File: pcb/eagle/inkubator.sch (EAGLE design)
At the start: 34 parts, among them Q1 BT138-600, Q2 BT138-600, U1 L78L33ABUTR, U2 MOC3063, U3 MOC3063

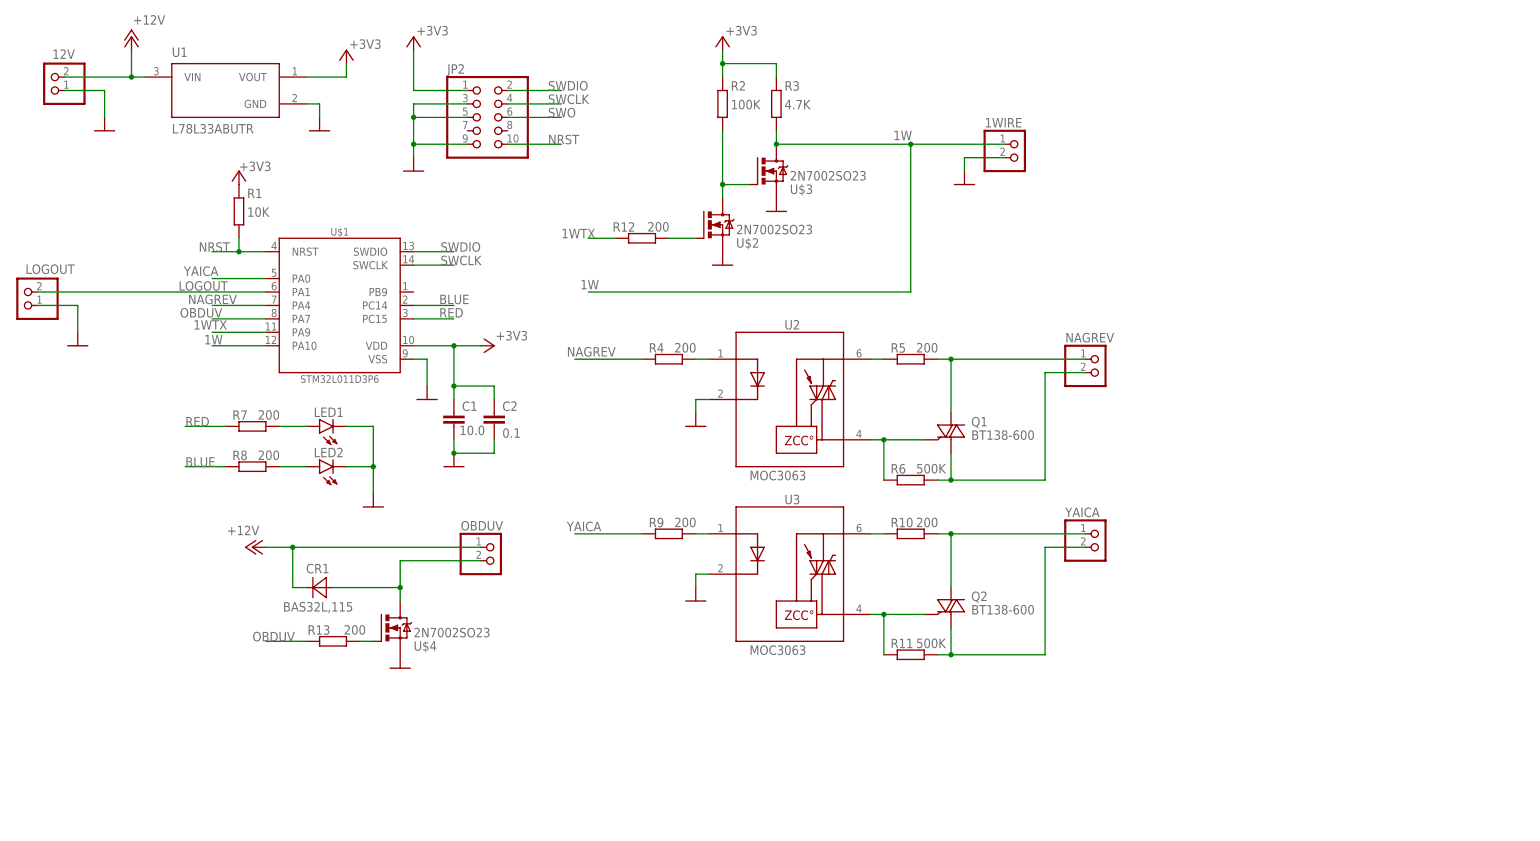
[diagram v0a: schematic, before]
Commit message: Рефакторинг принципиальной схемы и печатной платы
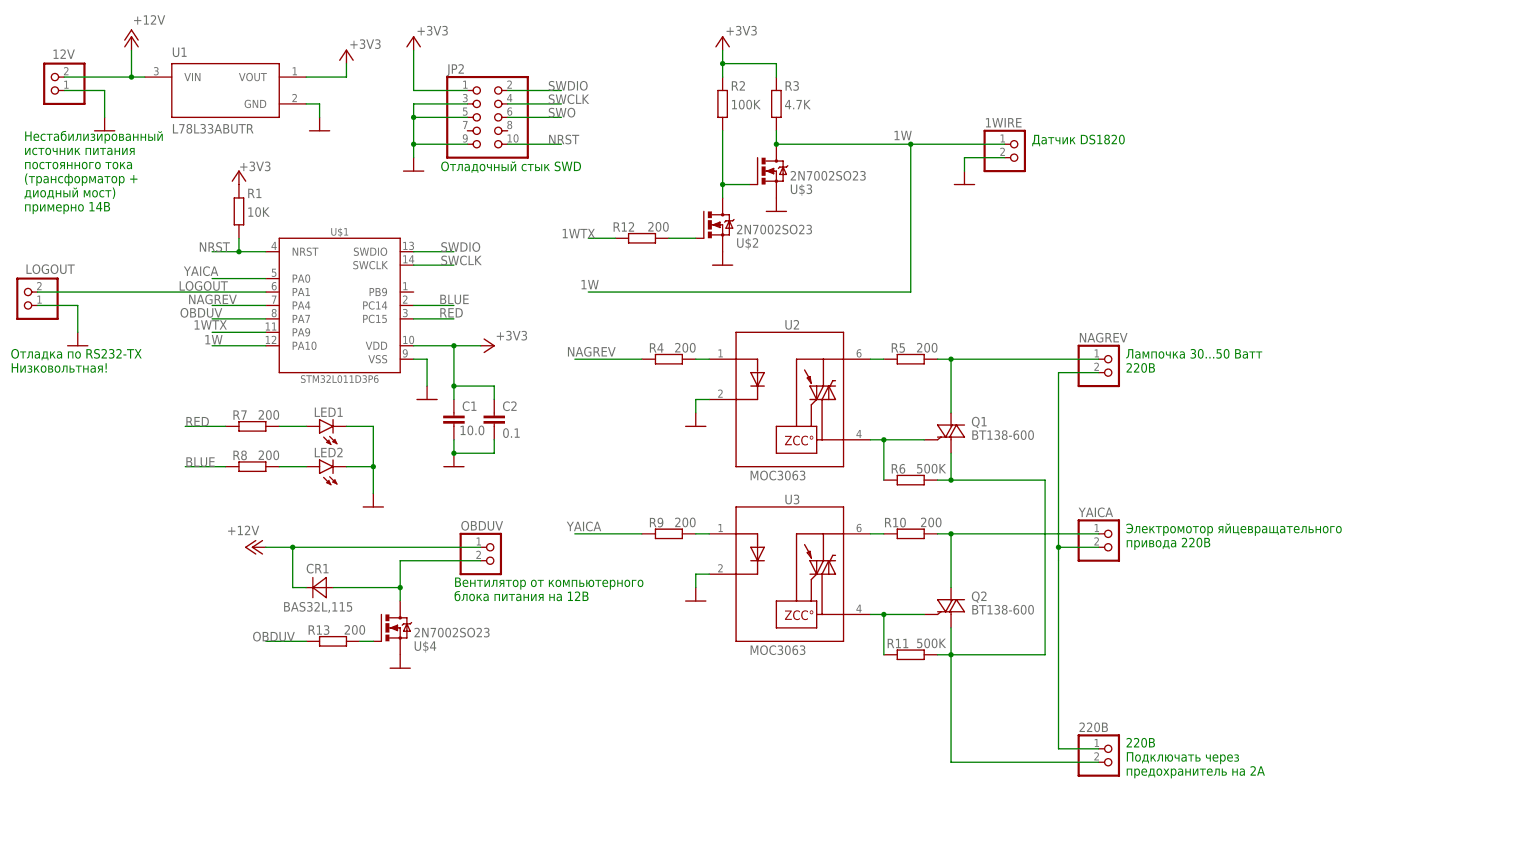
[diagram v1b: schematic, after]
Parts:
- added 220В: (no value), pinhead:PINHD-1X2
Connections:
- net N$13: now also 220В.2, Q1.A1, R6.1; no longer YAICA.2
- net N$6: now also 220В.1, YAICA.2; no longer Q1.A1, R6.1
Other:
- note added: "220В Подключать через предохранитель на 2А"
- note added: "Вентилятор от компьютерного блока питания на 12В"
- note added: "Датчик DS1820"
- note added: "Лампочка 30...50 Ватт 220В"
- note added: "Нестабилизированный источник питания постоянного тока (трансформатор + диодный мост) примерно 14В"
- note added: "Отладка по RS232-TX Низковольтная!"
- note added: "Отладочный стык SWD"
- note added: "Электромотор яйцевращательного привода 220В"
- moved on the sheet: NAGREV, YAICA
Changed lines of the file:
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@@
 <part name="LOGOUT" library="pinhead" library_urn="urn:adsk.eagle:library:325" deviceset="PINHD-1X2" device="" package3d_urn="urn:adsk.eagle:package:22435/2"/>
 <part name="GND13" library="supply1" library_urn="urn:adsk.eagle:library:371" deviceset="GND" device=""/>
+<part name="220В" library="pinhead" library_urn="urn:adsk.eagle:library:325" deviceset="PINHD-1X2" device="" package3d_urn="urn:adsk.eagle:package:22435/2"/>
 </parts>
 <sheets>
 <sheet>
 <plain>
+<text x="193.04" y="55.88" size="1.778" layer="91">Лампочка 30...50 Ватт
+220В</text>
+<text x="193.04" y="22.86" size="1.778" layer="91">Электромотор яйцевращательного
+привода 220В</text>
+<text x="175.26" y="99.06" size="1.778" layer="91">Датчик DS1820</text>
+<text x="66.04" y="12.7" size="1.778" layer="91">Вентилятор от компьютерного
+блока питания на 12В</text>
+<text x="-17.78" y="55.88" size="1.778" layer="91">Отладка по RS232-TX
+Низковольтная!</text>
+<text x="-15.24" y="86.36" size="1.778" layer="91">Нестабилизированный
+источник питания
+постоянного тока
+(трансформатор +
+диодный мост)
+примерно 14В</text>
+<text x="63.5" y="93.98" size="1.778" layer="91">Отладочный стык SWD</text>
+<text x="193.04" y="-20.32" size="1.778" layer="91">220В
+Подключать через
+предохранитель на 2А</text>
 </plain>
 <instances>
@@
 </instance>
 <instance part="GND8" gate="1" x="162.56" y="91.44" smashed="yes"/>
-<instance part="NAGREV" gate="G$1" x="187.96" y="55.88" smashed="yes">
-<attribute name="NAME" x="181.61" y="61.595" size="1.778" layer="95"/>
-<attribute name="VALUE" x="181.61" y="50.8" size="1.778" layer="96"/>
+<instance part="NAGREV" gate="G$1" x="190.5" y="55.88" smashed="yes">
+<attribute name="NAME" x="184.15" y="61.595" size="1.778" layer="95"/>
+<attribute name="VALUE" x="184.15" y="50.8" size="1.778" layer="96"/>
 </instance>
 <instance part="U3" gate="G$1" x="129.54" y="17.78" smashed="yes">
@@
 </instance>
 <instance part="R10" gate="G$1" x="152.4" y="25.4" smashed="yes" rot="R180">
-<attribute name="NAME" x="148.59" y="26.6446" size="1.778" layer="95"/>
-<attribute name="VALUE" x="153.416" y="26.67" size="1.778" layer="96"/>
+<attribute name="NAME" x="147.32" y="26.6446" size="1.778" layer="95"/>
+<attribute name="VALUE" x="154.178" y="26.67" size="1.778" layer="96"/>
 </instance>
 <instance part="R11" gate="G$1" x="152.4" y="2.54" smashed="yes" rot="R180">
-<attribute name="NAME" x="148.59" y="3.7846" size="1.778" layer="95"/>
+<attribute name="NAME" x="147.828" y="3.7846" size="1.778" layer="95"/>
 <attribute name="VALUE" x="153.416" y="3.81" size="1.778" layer="96"/>
 </instance>
-<instance part="YAICA" gate="G$1" x="187.96" y="22.86" smashed="yes">
-<attribute name="NAME" x="181.61" y="28.575" size="1.778" layer="95"/>
-<attribute name="VALUE" x="181.61" y="17.78" size="1.778" layer="96"/>
+<instance part="YAICA" gate="G$1" x="190.5" y="22.86" smashed="yes">
+<attribute name="NAME" x="184.15" y="28.575" size="1.778" layer="95"/>
+<attribute name="VALUE" x="184.15" y="17.78" size="1.778" layer="96"/>
 </instance>
 <instance part="U$4" gate="G$1" x="53.34" y="7.62" smashed="yes" rot="MR180">
@@
 </instance>
 <instance part="GND13" gate="1" x="-5.08" y="60.96" smashed="yes"/>
+<instance part="220В" gate="G$1" x="190.5" y="-17.78" smashed="yes">
+<attribute name="NAME" x="184.15" y="-12.065" size="1.778" layer="95"/>
+<attribute name="VALUE" x="184.15" y="-22.86" size="1.778" layer="96"/>
+</instance>
 </instances>
 <busses>
@@
 <pinref part="Q1" gate="G$1" pin="A2"/>
 <wire x1="160.02" y1="58.42" x2="160.02" y2="48.26" width="0.1524" layer="91"/>
-<wire x1="160.02" y1="58.42" x2="185.42" y2="58.42" width="0.1524" layer="91"/>
+<wire x1="160.02" y1="58.42" x2="187.96" y2="58.42" width="0.1524" layer="91"/>
 <junction x="160.02" y="58.42"/>
 <pinref part="NAGREV" gate="G$1" pin="1"/>
-</segment>
-</net>
-<net name="N$6" class="0">
-<segment>
-<pinref part="R6" gate="G$1" pin="1"/>
-<wire x1="157.48" y1="35.56" x2="160.02" y2="35.56" width="0.1524" layer="91"/>
-<pinref part="Q1" gate="G$1" pin="A1"/>
-<wire x1="160.02" y1="35.56" x2="160.02" y2="40.64" width="0.1524" layer="91"/>
-<wire x1="160.02" y1="35.56" x2="177.8" y2="35.56" width="0.1524" layer="91"/>
-<junction x="160.02" y="35.56"/>
-<pinref part="NAGREV" gate="G$1" pin="2"/>
-<wire x1="185.42" y1="55.88" x2="177.8" y2="55.88" width="0.1524" layer="91"/>
-<wire x1="177.8" y1="55.88" x2="177.8" y2="35.56" width="0.1524" layer="91"/>
 </segment>
 </net>
@@
 <pinref part="Q2" gate="G$1" pin="A2"/>
 <wire x1="160.02" y1="25.4" x2="160.02" y2="15.24" width="0.1524" layer="91"/>
-<wire x1="160.02" y1="25.4" x2="185.42" y2="25.4" width="0.1524" layer="91"/>
+<wire x1="160.02" y1="25.4" x2="187.96" y2="25.4" width="0.1524" layer="91"/>
 <junction x="160.02" y="25.4"/>
 <pinref part="YAICA" gate="G$1" pin="1"/>
@@
 <pinref part="Q2" gate="G$1" pin="A1"/>
 <wire x1="160.02" y1="2.54" x2="160.02" y2="7.62" width="0.1524" layer="91"/>
+<pinref part="R6" gate="G$1" pin="1"/>
+<wire x1="157.48" y1="35.56" x2="160.02" y2="35.56" width="0.1524" layer="91"/>
+<pinref part="Q1" gate="G$1" pin="A1"/>
+<wire x1="160.02" y1="35.56" x2="160.02" y2="40.64" width="0.1524" layer="91"/>
+<wire x1="177.8" y1="2.54" x2="177.8" y2="35.56" width="0.1524" layer="91"/>
+<wire x1="177.8" y1="35.56" x2="160.02" y2="35.56" width="0.1524" layer="91"/>
+<junction x="160.02" y="35.56"/>
 <wire x1="160.02" y1="2.54" x2="177.8" y2="2.54" width="0.1524" layer="91"/>
 <junction x="160.02" y="2.54"/>
-<pinref part="YAICA" gate="G$1" pin="2"/>
-<wire x1="185.42" y1="22.86" x2="177.8" y2="22.86" width="0.1524" layer="91"/>
-<wire x1="177.8" y1="22.86" x2="177.8" y2="2.54" width="0.1524" layer="91"/>
+<wire x1="160.02" y1="2.54" x2="160.02" y2="-17.78" width="0.1524" layer="91"/>
+<pinref part="220В" gate="G$1" pin="2"/>
+<wire x1="160.02" y1="-17.78" x2="187.96" y2="-17.78" width="0.1524" layer="91"/>
 </segment>
 </net>
@@
 </segment>
 </net>
+<net name="N$6" class="0">
+<segment>
+<pinref part="220В" gate="G$1" pin="1"/>
+<wire x1="187.96" y1="-15.24" x2="180.34" y2="-15.24" width="0.1524" layer="91"/>
+<wire x1="180.34" y1="-15.24" x2="180.34" y2="20.32" width="0.1524" layer="91"/>
+<pinref part="NAGREV" gate="G$1" pin="2"/>
+<wire x1="180.34" y1="22.86" x2="180.34" y2="55.88" width="0.1524" layer="91"/>
+<wire x1="180.34" y1="55.88" x2="187.96" y2="55.88" width="0.1524" layer="91"/>
+<pinref part="YAICA" gate="G$1" pin="2"/>
+<wire x1="187.96" y1="22.86" x2="180.34" y2="22.86" width="0.1524" layer="91"/>
+<wire x1="180.34" y1="22.86" x2="180.34" y2="20.32" width="0.1524" layer="91"/>
+<junction x="180.34" y="22.86"/>
+</segment>
+</net>
 </nets>
 </sheet>
@@
 </drawing>
 <compatibility>
+<note version="6.3" minversion="6.2.2" severity="warning">
+Since Version 6.2.2 text objects can contain more than one line,
+which will not be processed correctly with this version.
+</note>
 <note version="8.2" severity="warning">
 Since Version 8.2, EAGLE supports online libraries. The ids

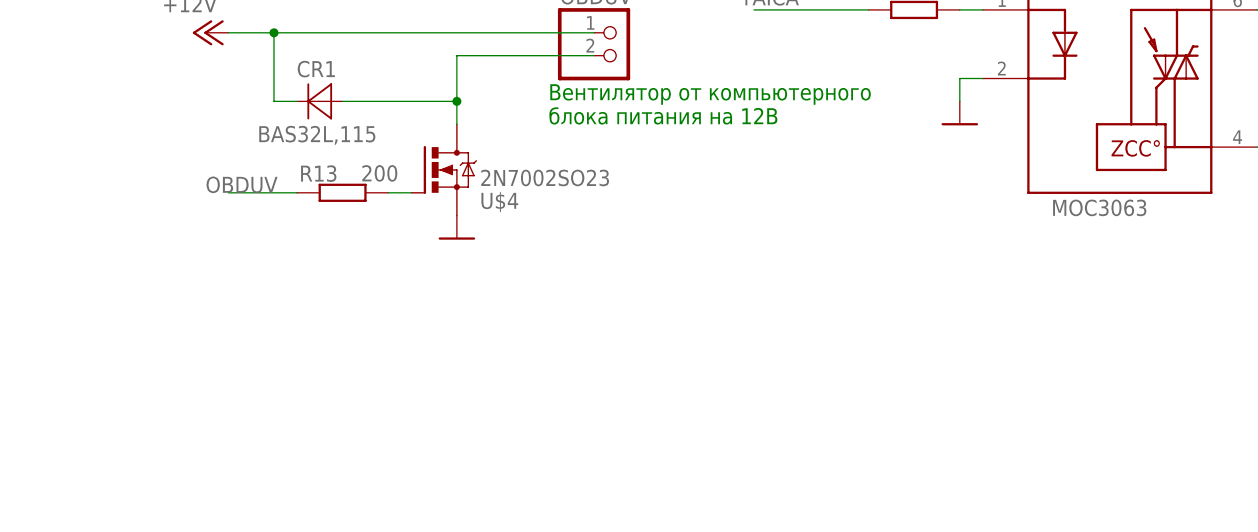
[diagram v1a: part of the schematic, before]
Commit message: Добавлен узел управления 12-и вольтовым мотором привода яйцекрутилки, для случая если мотор DC 12V
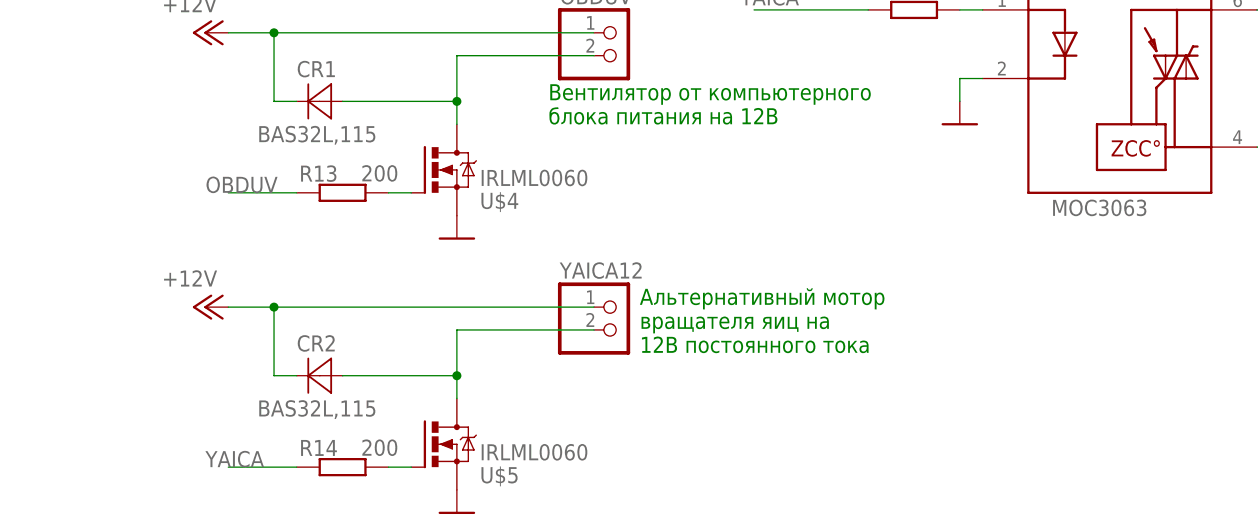
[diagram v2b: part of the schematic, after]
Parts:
- added CR2: BAS32L,115, BAS32L_115:BAS32L,115
- added R14: 200, resistor:R-EU_R0603
- added U$5: IRLML0060, 2n7002:2N7002SO23
- added YAICA12: (no value), pinhead:PINHD-1X2
- U$4: value 2N7002SO23 -> IRLML0060
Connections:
- new net N$17: R14.1, U$5.G
- new net N$18: CR2.ANODE, U$5.D, YAICA12.2
- net +12V: now also CR2.CATHODE, YAICA12.1
- net GND: now also U$5.S
- net YAICA: now also R14.2
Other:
- note added: "Альтернативный мотор вращателя яиц на 12В постоянного тока"
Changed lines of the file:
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@@
 <part name="R11" library="resistor" library_urn="urn:adsk.eagle:library:348" deviceset="R-EU_" device="R1206" package3d_urn="urn:adsk.eagle:package:23540/2" value="500K"/>
 <part name="YAICA" library="pinhead" library_urn="urn:adsk.eagle:library:325" deviceset="PINHD-1X2" device="" package3d_urn="urn:adsk.eagle:package:22435/2"/>
-<part name="U$4" library="2n7002" deviceset="2N7002" device="SO23" package3d_urn="urn:adsk.eagle:package:28738/2"/>
+<part name="U$4" library="2n7002" deviceset="2N7002" device="SO23" package3d_urn="urn:adsk.eagle:package:28738/2" value="IRLML0060"/>
 <part name="GND10" library="supply1" library_urn="urn:adsk.eagle:library:371" deviceset="GND" device=""/>
 <part name="R12" library="resistor" library_urn="urn:adsk.eagle:library:348" deviceset="R-EU_" device="R0603" package3d_urn="urn:adsk.eagle:package:23555/3" value="200"/>
@@
 <part name="GND13" library="supply1" library_urn="urn:adsk.eagle:library:371" deviceset="GND" device=""/>
 <part name="220В" library="pinhead" library_urn="urn:adsk.eagle:library:325" deviceset="PINHD-1X2" device="" package3d_urn="urn:adsk.eagle:package:22435/2"/>
+<part name="U$5" library="2n7002" deviceset="2N7002" device="SO23" package3d_urn="urn:adsk.eagle:package:28738/2" value="IRLML0060"/>
+<part name="GND14" library="supply1" library_urn="urn:adsk.eagle:library:371" deviceset="GND" device=""/>
+<part name="R14" library="resistor" library_urn="urn:adsk.eagle:library:348" deviceset="R-EU_" device="R0603" package3d_urn="urn:adsk.eagle:package:23555/3" value="200"/>
+<part name="YAICA12" library="pinhead" library_urn="urn:adsk.eagle:library:325" deviceset="PINHD-1X2" device="" package3d_urn="urn:adsk.eagle:package:22435/2"/>
+<part name="CR2" library="BAS32L_115" deviceset="BAS32L,115" device=""/>
+<part name="P+3" library="supply1" library_urn="urn:adsk.eagle:library:371" deviceset="+12V" device=""/>
 </parts>
 <sheets>
@@
 Подключать через
 предохранитель на 2А</text>
+<text x="76.2" y="-12.7" size="1.778" layer="91">Альтернативный мотор
+вращателя яиц на
+12В постоянного тока</text>
 </plain>
 <instances>
@@
 <attribute name="NAME" x="184.15" y="-12.065" size="1.778" layer="95"/>
 <attribute name="VALUE" x="184.15" y="-22.86" size="1.778" layer="96"/>
+</instance>
+<instance part="U$5" gate="G$1" x="53.34" y="-22.86" smashed="yes" rot="MR180">
+<attribute name="NAME" x="58.42" y="-25.4" size="1.778" layer="95" rot="MR180"/>
+<attribute name="VALUE" x="58.42" y="-22.86" size="1.778" layer="96" rot="MR180"/>
+</instance>
+<instance part="GND14" gate="1" x="55.88" y="-30.48" smashed="yes"/>
+<instance part="R14" gate="G$1" x="43.18" y="-25.4" smashed="yes" rot="R180">
+<attribute name="NAME" x="38.354" y="-24.1554" size="1.778" layer="95"/>
+<attribute name="VALUE" x="45.212" y="-24.13" size="1.778" layer="96"/>
+</instance>
+<instance part="YAICA12" gate="G$1" x="73.66" y="-10.16" smashed="yes">
+<attribute name="NAME" x="67.31" y="-4.445" size="1.778" layer="95"/>
+<attribute name="VALUE" x="67.31" y="-15.24" size="1.778" layer="96"/>
+</instance>
+<instance part="CR2" gate="A" x="40.64" y="-15.24" smashed="yes" rot="R180">
+<attribute name="VALUE" x="33.707040625" y="-19.76891875" size="1.778" layer="96" ratio="10" rot="SR0"/>
+<attribute name="NAME" x="38.07408125" y="-12.542590625" size="1.778" layer="95" ratio="10" rot="SR0"/>
+</instance>
+<instance part="P+3" gate="1" x="27.94" y="-7.62" smashed="yes" rot="R90">
+<attribute name="VALUE" x="23.114" y="-5.334" size="1.778" layer="96"/>
 </instance>
 </instances>
@@
 <wire x1="-5.08" y1="68.58" x2="-12.7" y2="68.58" width="0.1524" layer="91"/>
 </segment>
+<segment>
+<pinref part="GND14" gate="1" pin="GND"/>
+<pinref part="U$5" gate="G$1" pin="S"/>
+</segment>
 </net>
 <net name="SWCLK" class="0">
@@
 <wire x1="101.6" y1="25.4" x2="88.9" y2="25.4" width="0.1524" layer="91"/>
 <label x="87.376" y="25.908" size="1.778" layer="95"/>
+</segment>
+<segment>
+<pinref part="R14" gate="G$1" pin="2"/>
+<wire x1="38.1" y1="-25.4" x2="30.48" y2="-25.4" width="0.1524" layer="91"/>
+<label x="27.94" y="-25.4" size="1.778" layer="95"/>
 </segment>
 </net>
@@
 <pinref part="P+2" gate="1" pin="+12V"/>
 </segment>
+<segment>
+<pinref part="YAICA12" gate="G$1" pin="1"/>
+<wire x1="71.12" y1="-7.62" x2="35.56" y2="-7.62" width="0.1524" layer="91"/>
+<pinref part="CR2" gate="A" pin="CATHODE"/>
+<wire x1="35.56" y1="-7.62" x2="30.48" y2="-7.62" width="0.1524" layer="91"/>
+<wire x1="38.1" y1="-15.24" x2="35.56" y2="-15.24" width="0.1524" layer="91"/>
+<wire x1="35.56" y1="-15.24" x2="35.56" y2="-7.62" width="0.1524" layer="91"/>
+<junction x="35.56" y="-7.62"/>
+<pinref part="P+3" gate="1" pin="+12V"/>
+</segment>
 </net>
 <net name="N$6" class="0">
@@
 </segment>
 </net>
+<net name="N$17" class="0">
+<segment>
+<pinref part="R14" gate="G$1" pin="1"/>
+<pinref part="U$5" gate="G$1" pin="G"/>
+<wire x1="48.26" y1="-25.4" x2="50.8" y2="-25.4" width="0.1524" layer="91"/>
+</segment>
+</net>
+<net name="N$18" class="0">
+<segment>
+<pinref part="U$5" gate="G$1" pin="D"/>
+<wire x1="55.88" y1="-17.78" x2="55.88" y2="-15.24" width="0.1524" layer="91"/>
+<pinref part="YAICA12" gate="G$1" pin="2"/>
+<wire x1="55.88" y1="-15.24" x2="55.88" y2="-10.16" width="0.1524" layer="91"/>
+<wire x1="55.88" y1="-10.16" x2="71.12" y2="-10.16" width="0.1524" layer="91"/>
+<pinref part="CR2" gate="A" pin="ANODE"/>
+<wire x1="43.18" y1="-15.24" x2="55.88" y2="-15.24" width="0.1524" layer="91"/>
+<junction x="55.88" y="-15.24"/>
+</segment>
+</net>
